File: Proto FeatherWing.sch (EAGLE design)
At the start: 3 parts

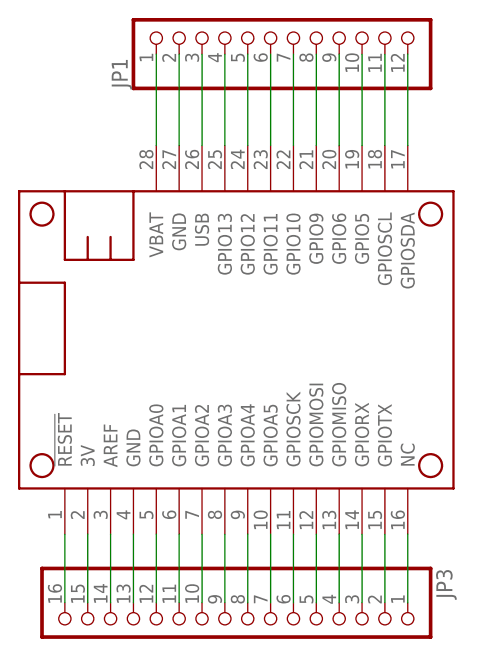
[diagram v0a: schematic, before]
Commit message: fix minor hole location error - EN is now labeled EN
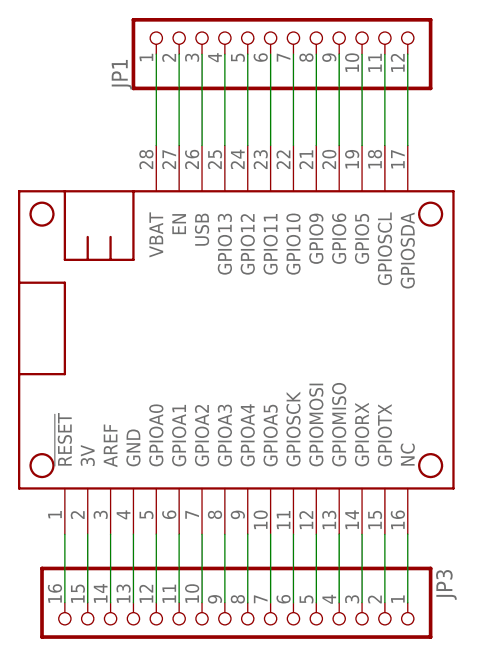
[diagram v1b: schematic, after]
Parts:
- MS1: value MICROSHIELD_NODIM -> FEATHERWING; device microbuilder:MICROSHIELD_NODIM -> microbuilder:FEATHERWING
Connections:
- net N$1: now also MS1.EN; no longer MS1.GND@1
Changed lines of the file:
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@@
 <grid distance="0.1" unitdist="inch" unit="inch" style="lines" multiple="1" display="no" altdistance="0.01" altunitdist="inch" altunit="inch"/>
 <layers>
-<layer number="1" name="Top" color="4" fill="1" visible="yes" active="no"/>
-<layer number="2" name="Route2" color="1" fill="3" visible="yes" active="no"/>
-<layer number="3" name="Route3" color="4" fill="3" visible="yes" active="no"/>
-<layer number="4" name="Route4" color="1" fill="4" visible="yes" active="no"/>
-<layer number="5" name="Route5" color="4" fill="4" visible="yes" active="no"/>
-<layer number="6" name="Route6" color="1" fill="8" visible="yes" active="no"/>
-<layer number="7" name="Route7" color="4" fill="8" visible="yes" active="no"/>
-<layer number="8" name="Route8" color="1" fill="2" visible="yes" active="no"/>
-<layer number="9" name="Route9" color="4" fill="2" visible="yes" active="no"/>
-<layer number="10" name="Route10" color="1" fill="7" visible="yes" active="no"/>
-<layer number="11" name="Route11" color="4" fill="7" visible="yes" active="no"/>
-<layer number="12" name="Route12" color="1" fill="5" visible="yes" active="no"/>
-<layer number="13" name="Route13" color="4" fill="5" visible="yes" active="no"/>
-<layer number="14" name="Route14" color="1" fill="6" visible="yes" active="no"/>
-<layer number="15" name="Route15" color="4" fill="6" visible="yes" active="no"/>
-<layer number="16" name="Bottom" color="1" fill="1" visible="yes" active="no"/>
-<layer number="17" name="Pads" color="2" fill="1" visible="yes" active="no"/>
-<layer number="18" name="Vias" color="2" fill="1" visible="yes" active="no"/>
-<layer number="19" name="Unrouted" color="6" fill="1" visible="yes" active="no"/>
-<layer number="20" name="Dimension" color="15" fill="1" visible="yes" active="no"/>
-<layer number="21" name="tPlace" color="14" fill="1" visible="yes" active="no"/>
-<layer number="22" name="bPlace" color="13" fill="1" visible="yes" active="no"/>
-<layer number="23" name="tOrigins" color="15" fill="1" visible="yes" active="no"/>
-<layer number="24" name="bOrigins" color="15" fill="1" visible="yes" active="no"/>
-<layer number="25" name="tNames" color="7" fill="1" visible="yes" active="no"/>
-<layer number="26" name="bNames" color="7" fill="1" visible="yes" active="no"/>
-<layer number="27" name="tValues" color="7" fill="1" visible="yes" active="no"/>
-<layer number="28" name="bValues" color="7" fill="1" visible="yes" active="no"/>
+<layer number="1" name="Top" color="4" fill="1" visible="no" active="no"/>
+<layer number="2" name="Route2" color="1" fill="3" visible="no" active="no"/>
+<layer number="3" name="Route3" color="4" fill="3" visible="no" active="no"/>
+<layer number="4" name="Route4" color="1" fill="4" visible="no" active="no"/>
+<layer number="5" name="Route5" color="4" fill="4" visible="no" active="no"/>
+<layer number="6" name="Route6" color="1" fill="8" visible="no" active="no"/>
+<layer number="7" name="Route7" color="4" fill="8" visible="no" active="no"/>
+<layer number="8" name="Route8" color="1" fill="2" visible="no" active="no"/>
+<layer number="9" name="Route9" color="4" fill="2" visible="no" active="no"/>
+<layer number="10" name="Route10" color="1" fill="7" visible="no" active="no"/>
+<layer number="11" name="Route11" color="4" fill="7" visible="no" active="no"/>
+<layer number="12" name="Route12" color="1" fill="5" visible="no" active="no"/>
+<layer number="13" name="Route13" color="4" fill="5" visible="no" active="no"/>
+<layer number="14" name="Route14" color="1" fill="6" visible="no" active="no"/>
+<layer number="15" name="Route15" color="4" fill="6" visible="no" active="no"/>
+<layer number="16" name="Bottom" color="1" fill="1" visible="no" active="no"/>
+<layer number="17" name="Pads" color="2" fill="1" visible="no" active="no"/>
+<layer number="18" name="Vias" color="2" fill="1" visible="no" active="no"/>
+<layer number="19" name="Unrouted" color="6" fill="1" visible="no" active="no"/>
+<layer number="20" name="Dimension" color="15" fill="1" visible="no" active="no"/>
+<layer number="21" name="tPlace" color="14" fill="1" visible="no" active="no"/>
+<layer number="22" name="bPlace" color="13" fill="1" visible="no" active="no"/>
+<layer number="23" name="tOrigins" color="15" fill="1" visible="no" active="no"/>
+<layer number="24" name="bOrigins" color="15" fill="1" visible="no" active="no"/>
+<layer number="25" name="tNames" color="7" fill="1" visible="no" active="no"/>
+<layer number="26" name="bNames" color="7" fill="1" visible="no" active="no"/>
+<layer number="27" name="tValues" color="7" fill="1" visible="no" active="no"/>
+<layer number="28" name="bValues" color="7" fill="1" visible="no" active="no"/>
 <layer number="29" name="tStop" color="7" fill="3" visible="no" active="no"/>
 <layer number="30" name="bStop" color="7" fill="6" visible="no" active="no"/>
@@
 <layer number="35" name="tGlue" color="7" fill="4" visible="no" active="no"/>
 <layer number="36" name="bGlue" color="7" fill="5" visible="no" active="no"/>
-<layer number="37" name="tTest" color="7" fill="1" visible="yes" active="no"/>
-<layer number="38" name="bTest" color="7" fill="1" visible="yes" active="no"/>
+<layer number="37" name="tTest" color="7" fill="1" visible="no" active="no"/>
+<layer number="38" name="bTest" color="7" fill="1" visible="no" active="no"/>
 <layer number="39" name="tKeepout" color="4" fill="11" visible="no" active="no"/>
 <layer number="40" name="bKeepout" color="1" fill="11" visible="no" active="no"/>
@@
 <layer number="44" name="Drills" color="7" fill="1" visible="no" active="no"/>
 <layer number="45" name="Holes" color="7" fill="1" visible="no" active="no"/>
-<layer number="46" name="Milling" color="3" fill="1" visible="yes" active="no"/>
-<layer number="47" name="Measures" color="7" fill="1" visible="yes" active="no"/>
-<layer number="48" name="Document" color="7" fill="1" visible="yes" active="no"/>
-<layer number="49" name="Reference" color="7" fill="1" visible="yes" active="no"/>
-<layer number="50" name="dxf" color="7" fill="1" visible="yes" active="no"/>
-<layer number="51" name="tDocu" color="7" fill="1" visible="yes" active="no"/>
-<layer number="52" name="bDocu" color="7" fill="1" visible="yes" active="no"/>
-<layer number="53" name="tGND_GNDA" color="7" fill="9" visible="yes" active="no"/>
-<layer number="54" name="bGND_GNDA" color="1" fill="9" visible="yes" active="no"/>
-<layer number="56" name="wert" color="7" fill="1" visible="yes" active="no"/>
-<layer number="57" name="tCAD" color="7" fill="1" visible="yes" active="no"/>
-<layer number="59" name="tCarbon" color="7" fill="1" visible="yes" active="no"/>
-<layer number="60" name="bCarbon" color="7" fill="1" visible="yes" active="no"/>
+<layer number="46" name="Milling" color="3" fill="1" visible="no" active="no"/>
+<layer number="47" name="Measures" color="7" fill="1" visible="no" active="no"/>
+<layer number="48" name="Document" color="7" fill="1" visible="no" active="no"/>
+<layer number="49" name="Reference" color="7" fill="1" visible="no" active="no"/>
+<layer number="50" name="dxf" color="7" fill="1" visible="no" active="no"/>
+<layer number="51" name="tDocu" color="7" fill="1" visible="no" active="no"/>
+<layer number="52" name="bDocu" color="7" fill="1" visible="no" active="no"/>
+<layer number="53" name="tGND_GNDA" color="7" fill="9" visible="no" active="no"/>
+<layer number="54" name="bGND_GNDA" color="1" fill="9" visible="no" active="no"/>
+<layer number="56" name="wert" color="7" fill="1" visible="no" active="no"/>
+<layer number="57" name="tCAD" color="7" fill="1" visible="no" active="no"/>
+<layer number="59" name="tCarbon" color="7" fill="1" visible="no" active="no"/>
+<layer number="60" name="bCarbon" color="7" fill="1" visible="no" active="no"/>
 <layer number="90" name="Modules" color="7" fill="1" visible="no" active="yes"/>
 <layer number="91" name="Nets" color="2" fill="1" visible="yes" active="yes"/>
@@
 <parts>
 <part name="U$1" library="microbuilder" deviceset="FRAME_A4_ADAFRUIT" device=""/>
-<part name="MS1" library="microbuilder" deviceset="MICROSHIELD" device="_NODIM" value="MICROSHIELD_NODIM"/>
+<part name="MS1" library="microbuilder" deviceset="FEATHERWING" device="" value="FEATHERWING"/>
 <part name="JP3" library="microbuilder" deviceset="HEADER-1X16" device="_76MIL"/>
 <part name="JP1" library="microbuilder" deviceset="HEADER-1X12" device="76MIL"/>
@@
 <net name="N$1" class="0">
 <segment>
-<pinref part="MS1" gate="G$1" pin="GND@1"/>
+<pinref part="MS1" gate="G$1" pin="EN"/>
 <pinref part="JP1" gate="G$1" pin="2"/>
 <wire x1="93.98" y1="93.98" x2="93.98" y2="83.82" width="0.1524" layer="91"/>
